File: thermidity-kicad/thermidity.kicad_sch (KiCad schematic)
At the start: 21 parts, among them J1 Battery, J2 Display, J3 ISP, U1 ATmega328P-A, U2 MCP1501-30xSN, U3 TMP36GT9, U4 HIH-5030-001, Y1 32.768kHz Watch Crystal 10pF 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

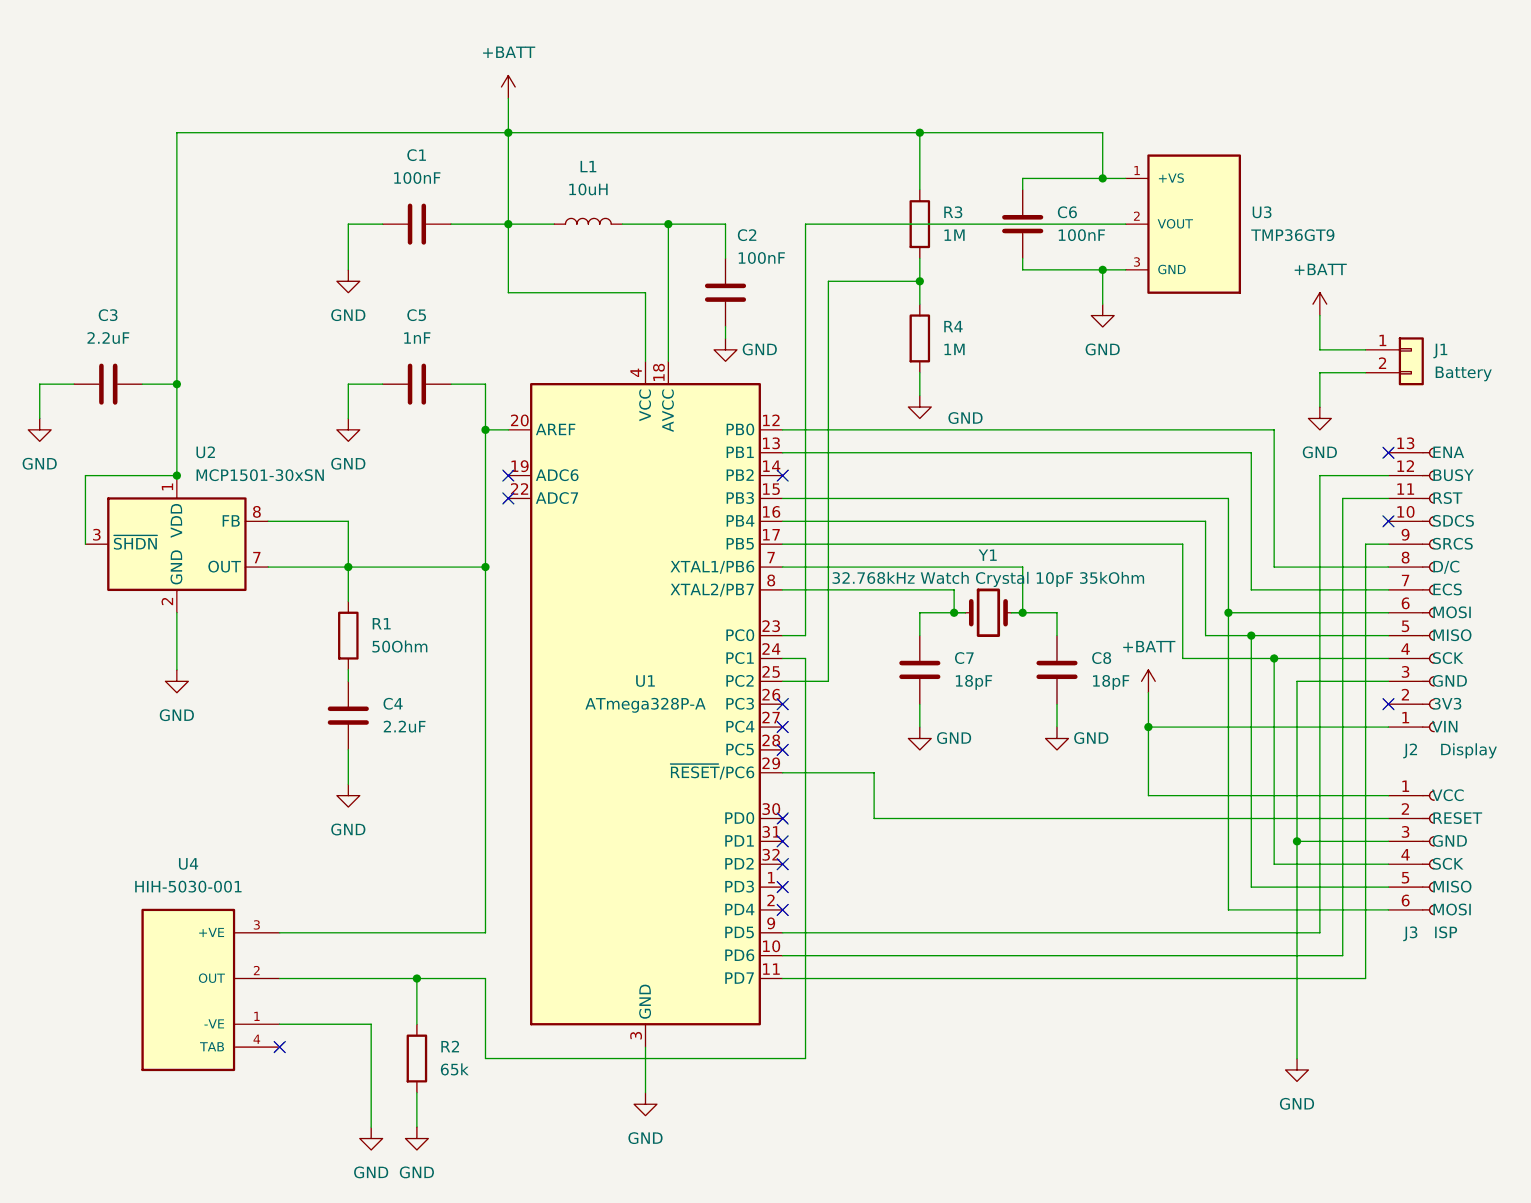
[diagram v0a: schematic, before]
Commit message: update README, schematic + PCB (remove crystal)
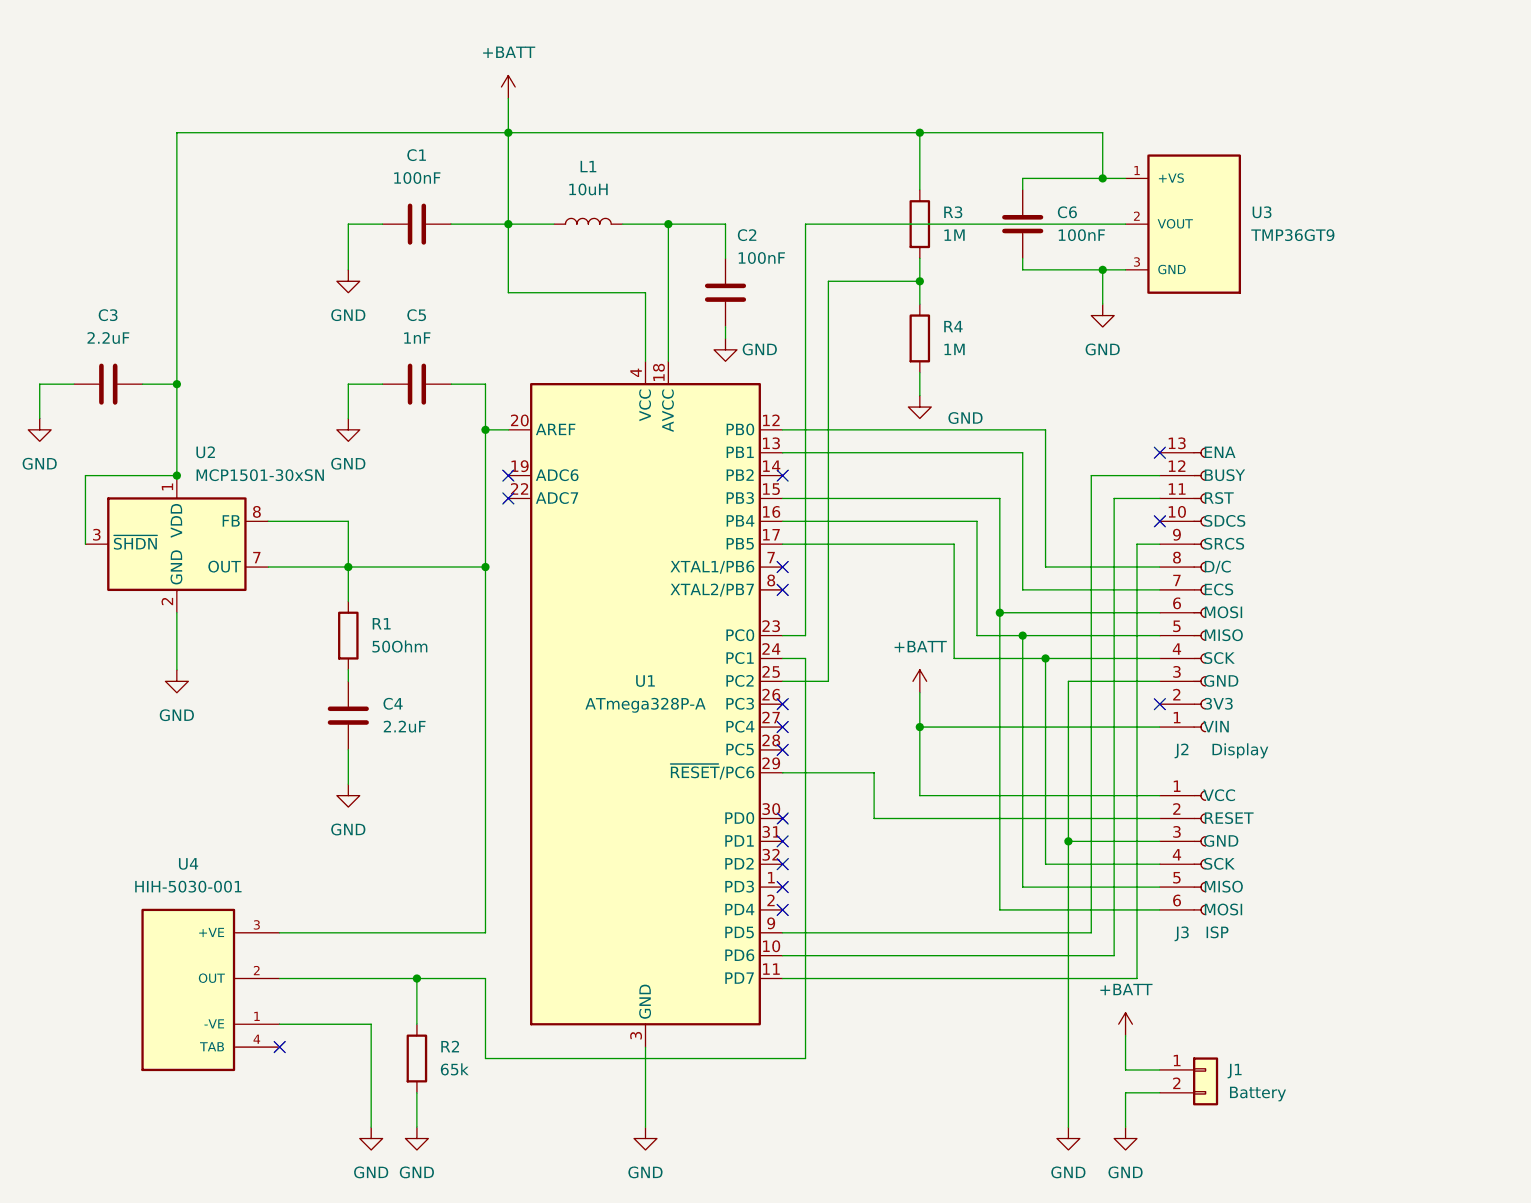
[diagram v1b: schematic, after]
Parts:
- removed C7, C8: 18pF, Capacitor_SMD:C_1206_3216Metric_Pad1.33x1.80mm_HandSolder, symbol Device:C
- removed Y1: 32.768kHz Watch Crystal 10pF 35kOhm, Crystal:Crystal_C38-LF_D3.0mm_L8.0mm_Horizontal, symbol Device:Crystal
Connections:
- no-connect marks 15 -> 17
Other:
- moved on the sheet: J1, J2, J3

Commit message: improve PCB, add comments
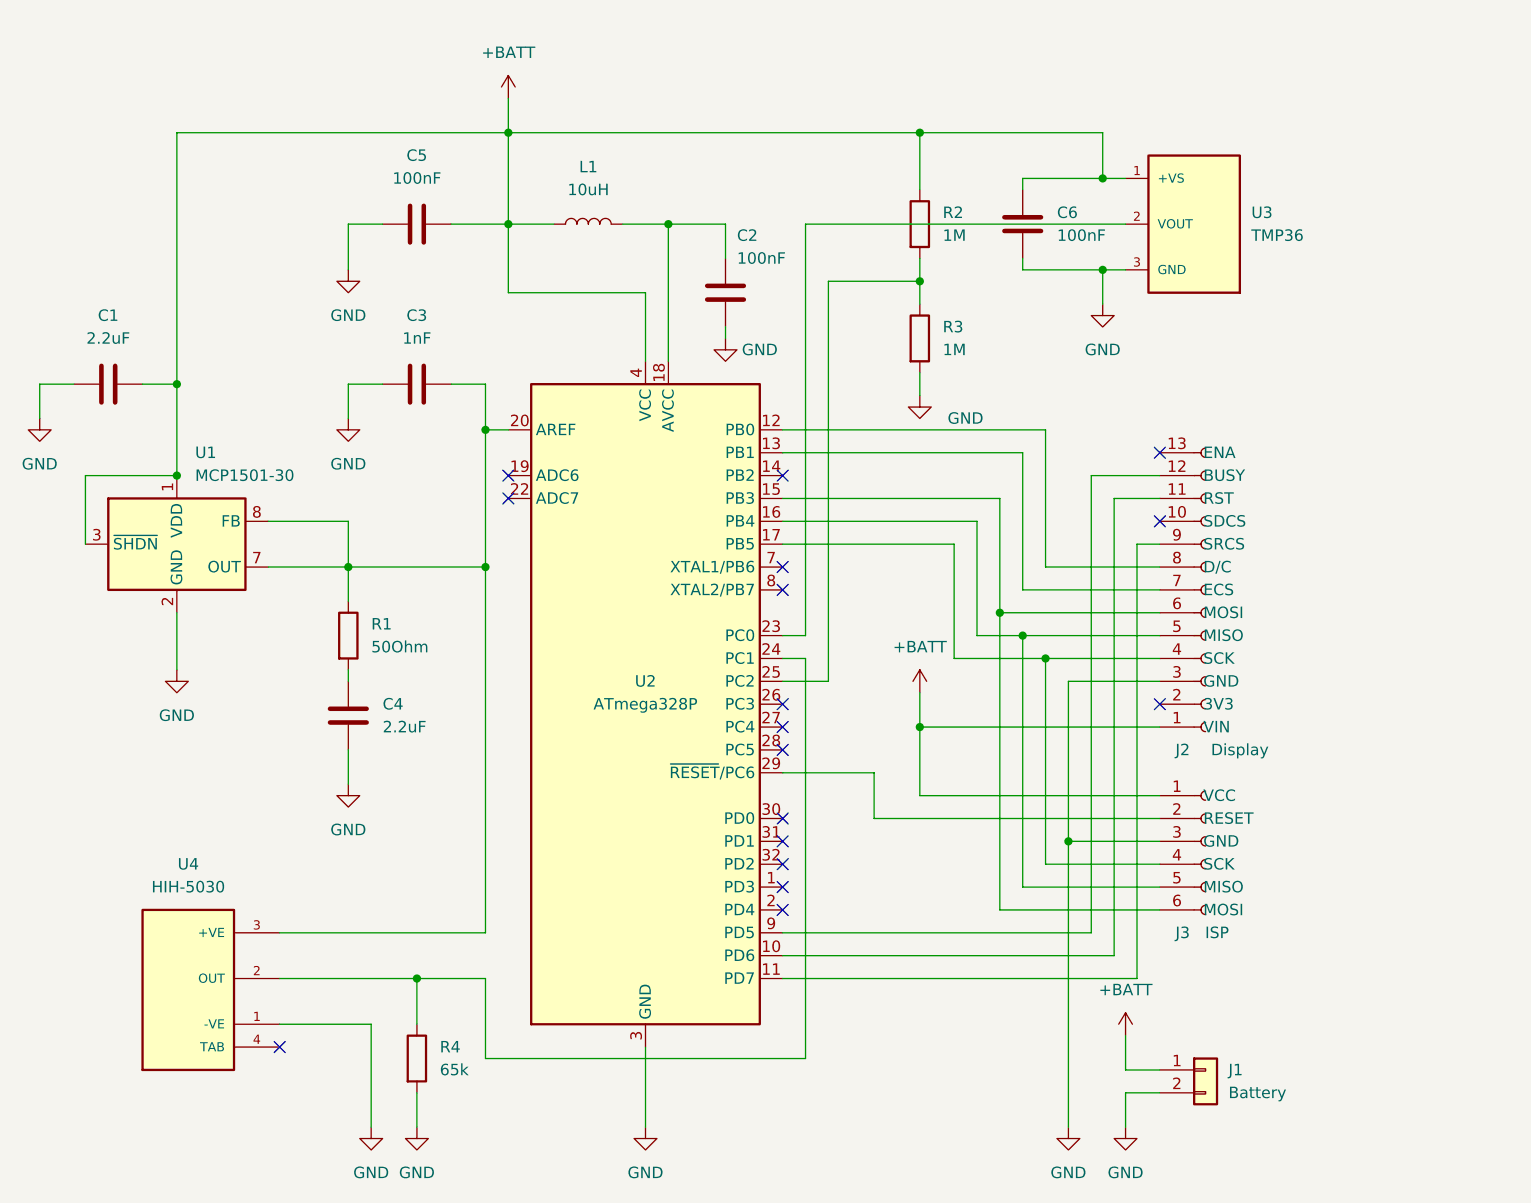
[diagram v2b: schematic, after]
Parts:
- U1: renamed from U2; value MCP1501-30xSN -> MCP1501-30
- U2: renamed from U1; value ATmega328P-A -> ATmega328P
- U3: value TMP36GT9 -> TMP36
- U4: value HIH-5030-001 -> HIH-5030
- renumbered C3 to C1, C5 to C3, C1 to C5, R3 to R2, R4 to R3, R2 to R4
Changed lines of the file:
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@@
   (symbol (lib_id "Device:C") (at 86.36 60.96 90) (unit 1)
     (in_bom yes) (on_board yes) (fields_autoplaced)
-    (property "Reference" "C3" (id 0) (at 86.36 53.34 90))
+    (property "Reference" "C1" (id 0) (at 86.36 53.34 90))
     (property "Value" "2.2uF" (id 1) (at 86.36 55.88 90))
     (property "Footprint" "Capacitor_SMD:C_1206_3216Metric_Pad1.33x1.80mm_HandSolder" (id 2) (at 90.17 59.9948 0)
@@
   (symbol (lib_id "Device:C") (at 120.65 43.18 90) (unit 1)
     (in_bom yes) (on_board yes) (fields_autoplaced)
-    (property "Reference" "C1" (id 0) (at 120.65 35.56 90))
+    (property "Reference" "C5" (id 0) (at 120.65 35.56 90))
     (property "Value" "100nF" (id 1) (at 120.65 38.1 90))
     (property "Footprint" "Capacitor_SMD:C_1206_3216Metric_Pad1.33x1.80mm_HandSolder" (id 2) (at 124.46 42.2148 0)
@@
   (symbol (lib_id "MCU_Microchip_ATmega:ATmega328P-A") (at 146.05 96.52 0) (unit 1)
     (in_bom yes) (on_board yes)
-    (property "Reference" "U1" (id 0) (at 146.05 93.98 0))
-    (property "Value" "ATmega328P-A" (id 1) (at 146.05 96.52 0))
+    (property "Reference" "U2" (id 0) (at 146.05 93.98 0))
+    (property "Value" "ATmega328P" (id 1) (at 146.05 96.52 0))
     (property "Footprint" "Package_QFP:TQFP-32_7x7mm_P0.8mm" (id 2) (at 146.05 96.52 0)
       (effects (font (size 1.27 1.27) italic) hide)
@@
   (symbol (lib_id "Reference_Voltage:MCP1501-30xSN") (at 93.98 78.74 0) (unit 1)
     (in_bom yes) (on_board yes) (fields_autoplaced)
-    (property "Reference" "U2" (id 0) (at 95.9994 68.58 0)
-      (effects (font (size 1.27 1.27)) (justify left))
-    )
-    (property "Value" "MCP1501-30xSN" (id 1) (at 95.9994 71.12 0)
+    (property "Reference" "U1" (id 0) (at 95.9994 68.58 0)
+      (effects (font (size 1.27 1.27)) (justify left))
+    )
+    (property "Value" "MCP1501-30" (id 1) (at 95.9994 71.12 0)
       (effects (font (size 1.27 1.27)) (justify left))
     )
@@
   (symbol (lib_id "Device:R") (at 120.65 135.89 0) (unit 1)
     (in_bom yes) (on_board yes) (fields_autoplaced)
-    (property "Reference" "R2" (id 0) (at 123.19 134.6199 0)
+    (property "Reference" "R4" (id 0) (at 123.19 134.6199 0)
       (effects (font (size 1.27 1.27)) (justify left))
     )
@@
       (effects (font (size 1.27 1.27)) (justify right))
     )
-    (property "Value" "TMP36GT9" (id 1) (at 213.36 44.4499 0)
+    (property "Value" "TMP36" (id 1) (at 213.36 44.4499 0)
       (effects (font (size 1.27 1.27)) (justify right))
     )
@@
   (symbol (lib_id "Device:R") (at 176.53 55.88 0) (unit 1)
     (in_bom yes) (on_board yes) (fields_autoplaced)
-    (property "Reference" "R4" (id 0) (at 179.07 54.6099 0)
+    (property "Reference" "R3" (id 0) (at 179.07 54.6099 0)
       (effects (font (size 1.27 1.27)) (justify left))
     )
@@
     (in_bom yes) (on_board yes) (fields_autoplaced)
     (property "Reference" "U4" (id 0) (at 95.25 114.3 0))
-    (property "Value" "HIH-5030-001" (id 1) (at 95.25 116.84 0))
+    (property "Value" "HIH-5030" (id 1) (at 95.25 116.84 0))
     (property "Footprint" "HIH-5030-001:HONEYWELL_HIH-5030-001" (id 2) (at 100.33 129.54 0)
       (effects (font (size 1.27 1.27)) (justify bottom) hide)
@@
   (symbol (lib_id "Device:R") (at 176.53 43.18 0) (unit 1)
     (in_bom yes) (on_board yes) (fields_autoplaced)
-    (property "Reference" "R3" (id 0) (at 179.07 41.9099 0)
+    (property "Reference" "R2" (id 0) (at 179.07 41.9099 0)
       (effects (font (size 1.27 1.27)) (justify left))
     )
@@
   (symbol (lib_id "Device:C") (at 120.65 60.96 90) (unit 1)
     (in_bom yes) (on_board yes) (fields_autoplaced)
-    (property "Reference" "C5" (id 0) (at 120.65 53.34 90))
+    (property "Reference" "C3" (id 0) (at 120.65 53.34 90))
     (property "Value" "1nF" (id 1) (at 120.65 55.88 90))
     (property "Footprint" "Capacitor_SMD:C_1206_3216Metric_Pad1.33x1.80mm_HandSolder" (id 2) (at 124.46 59.9948 0)
@@
       (reference "#PWR0117") (unit 1) (value "GND") (footprint "")
     )
-    (path "/8e459bfb-75fb-4c36-90af-73c840018779"
-      (reference "C1") (unit 1) (value "100nF") (footprint "Capacitor_SMD:C_1206_3216Metric_Pad1.33x1.80mm_HandSolder")
+    (path "/54ec993d-83da-4eca-be9d-cd16980aff27"
+      (reference "C1") (unit 1) (value "2.2uF") (footprint "Capacitor_SMD:C_1206_3216Metric_Pad1.33x1.80mm_HandSolder")
     )
     (path "/afc68921-ea8b-403a-9e3b-f2ef0af928a6"
       (reference "C2") (unit 1) (value "100nF") (footprint "Capacitor_SMD:C_1206_3216Metric_Pad1.33x1.80mm_HandSolder")
     )
-    (path "/54ec993d-83da-4eca-be9d-cd16980aff27"
-      (reference "C3") (unit 1) (value "2.2uF") (footprint "Capacitor_SMD:C_1206_3216Metric_Pad1.33x1.80mm_HandSolder")
+    (path "/fb41d1b8-7978-4471-8222-322ad33b566c"
+      (reference "C3") (unit 1) (value "1nF") (footprint "Capacitor_SMD:C_1206_3216Metric_Pad1.33x1.80mm_HandSolder")
     )
     (path "/106f1ff9-b877-44c2-b9bf-3e113e97f3ad"
       (reference "C4") (unit 1) (value "2.2uF") (footprint "Capacitor_SMD:C_1206_3216Metric_Pad1.33x1.80mm_HandSolder")
     )
-    (path "/fb41d1b8-7978-4471-8222-322ad33b566c"
-      (reference "C5") (unit 1) (value "1nF") (footprint "Capacitor_SMD:C_1206_3216Metric_Pad1.33x1.80mm_HandSolder")
+    (path "/8e459bfb-75fb-4c36-90af-73c840018779"
+      (reference "C5") (unit 1) (value "100nF") (footprint "Capacitor_SMD:C_1206_3216Metric_Pad1.33x1.80mm_HandSolder")
     )
     (path "/0178a398-4cac-462d-a5f8-54e853b1fa89"
@@
       (reference "R1") (unit 1) (value "50Ohm") (footprint "Resistor_SMD:R_0805_2012Metric_Pad1.20x1.40mm_HandSolder")
     )
+    (path "/f5367a98-6a53-432b-8730-086e1bb8663c"
+      (reference "R2") (unit 1) (value "1M") (footprint "Resistor_SMD:R_0805_2012Metric_Pad1.20x1.40mm_HandSolder")
+    )
+    (path "/d690645f-ce9c-4e4e-9a40-30e90181925c"
+      (reference "R3") (unit 1) (value "1M") (footprint "Resistor_SMD:R_0805_2012Metric_Pad1.20x1.40mm_HandSolder")
+    )
     (path "/ce63e81c-5d78-4d98-bb9e-4b0f5b9f1c49"
-      (reference "R2") (unit 1) (value "65k") (footprint "Resistor_SMD:R_0805_2012Metric_Pad1.20x1.40mm_HandSolder")
-    )
-    (path "/f5367a98-6a53-432b-8730-086e1bb8663c"
-      (reference "R3") (unit 1) (value "1M") (footprint "Resistor_SMD:R_0805_2012Metric_Pad1.20x1.40mm_HandSolder")
-    )
-    (path "/d690645f-ce9c-4e4e-9a40-30e90181925c"
-      (reference "R4") (unit 1) (value "1M") (footprint "Resistor_SMD:R_0805_2012Metric_Pad1.20x1.40mm_HandSolder")
+      (reference "R4") (unit 1) (value "65k") (footprint "Resistor_SMD:R_0805_2012Metric_Pad1.20x1.40mm_HandSolder")
+    )
+    (path "/c13bbeac-cd27-4dc9-ac13-971172caedb1"
+      (reference "U1") (unit 1) (value "MCP1501-30") (footprint "Package_SO:SOIC-8_3.9x4.9mm_P1.27mm")
     )
     (path "/a564f624-0149-43d3-9b25-20abc178b1e7"
-      (reference "U1") (unit 1) (value "ATmega328P-A") (footprint "Package_QFP:TQFP-32_7x7mm_P0.8mm")
-    )
-    (path "/c13bbeac-cd27-4dc9-ac13-971172caedb1"
-      (reference "U2") (unit 1) (value "MCP1501-30xSN") (footprint "Package_SO:SOIC-8_3.9x4.9mm_P1.27mm")
+      (reference "U2") (unit 1) (value "ATmega328P") (footprint "Package_QFP:TQFP-32_7x7mm_P0.8mm")
     )
     (path "/d57ede9f-d6ce-400c-b2ec-0a0c742662bf"
-      (reference "U3") (unit 1) (value "TMP36GT9") (footprint "TMP36GT9:XDCR_TMP36GT9")
+      (reference "U3") (unit 1) (value "TMP36") (footprint "TMP36GT9:XDCR_TMP36GT9")
     )
     (path "/e6831fa3-d0e2-442b-bad0-235e2cccce1e"
-      (reference "U4") (unit 1) (value "HIH-5030-001") (footprint "HIH-5030-001:HONEYWELL_HIH-5030-001")
-    )
-  )
+      (reference "U4") (unit 1) (value "HIH-5030") (footprint "HIH-5030-001:HONEYWELL_HIH-5030-001")
+    )
+  )

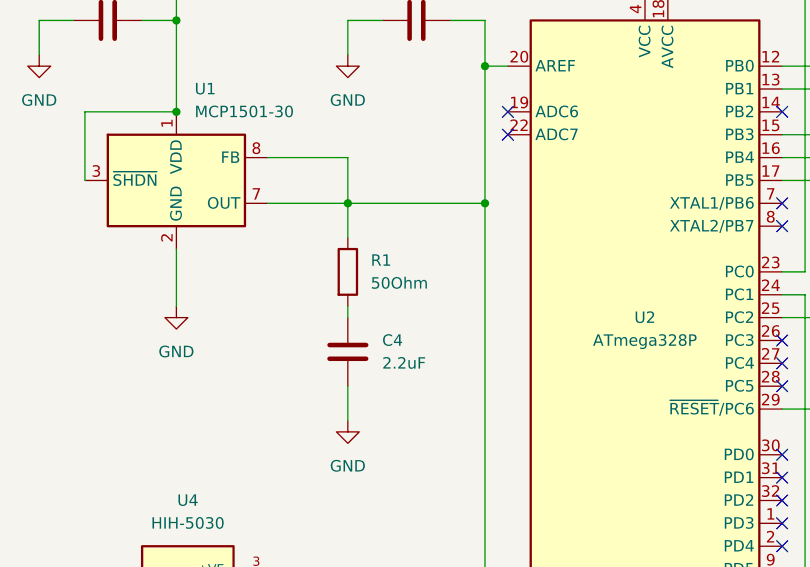
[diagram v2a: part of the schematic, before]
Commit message: improve PCB, add comments
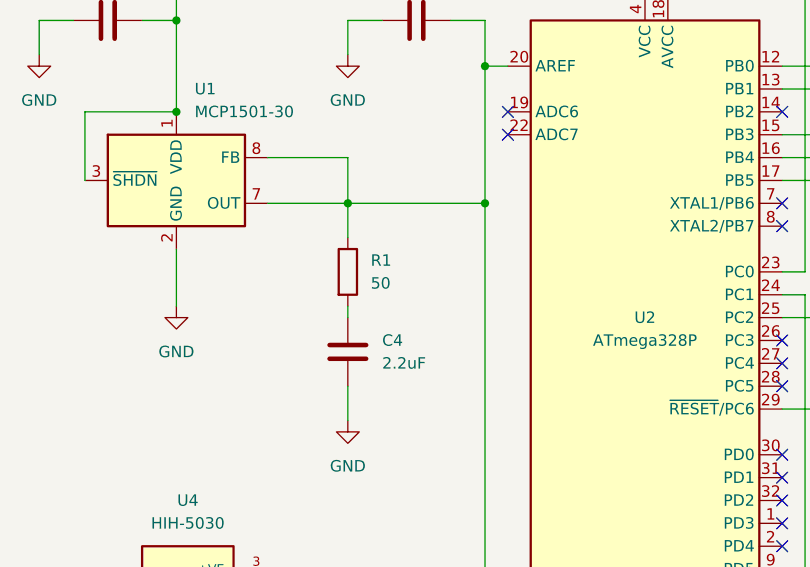
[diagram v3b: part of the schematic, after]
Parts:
- R1: value 50Ohm -> 50
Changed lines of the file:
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@@
       (effects (font (size 1.27 1.27)) (justify left))
     )
-    (property "Value" "50Ohm" (id 1) (at 115.57 90.17 0)
+    (property "Value" "50" (id 1) (at 115.57 90.17 0)
       (effects (font (size 1.27 1.27)) (justify left))
     )
@@
     )
     (path "/a1649bf0-4238-4971-a6f5-29c9840d4c56"
-      (reference "R1") (unit 1) (value "50Ohm") (footprint "Resistor_SMD:R_0805_2012Metric_Pad1.20x1.40mm_HandSolder")
+      (reference "R1") (unit 1) (value "50") (footprint "Resistor_SMD:R_0805_2012Metric_Pad1.20x1.40mm_HandSolder")
     )
     (path "/f5367a98-6a53-432b-8730-086e1bb8663c"
